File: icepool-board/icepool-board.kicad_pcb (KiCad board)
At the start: 4 copper layers, 90 x 40 mm, 103 parts, among them J2 PWR_IN, J3 I2C, J4 SWD, J5 8P8C_Shielded, J6 8P8C_Shielded, J7 USB_B_Micro, SW1 B3U-1000P, U1 LD1117S33CTR, U2 LD1117S12CTR, U3 ATSAMD21E, U4 ISL83488/ISL83490, U5 iCE40HX8K-BG121(121-Ball_caBG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, U6 iCE40HX8K-BG121(121-Ball_caBG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, X1 CB3LV-3I-16M0000, Y1 16MHz

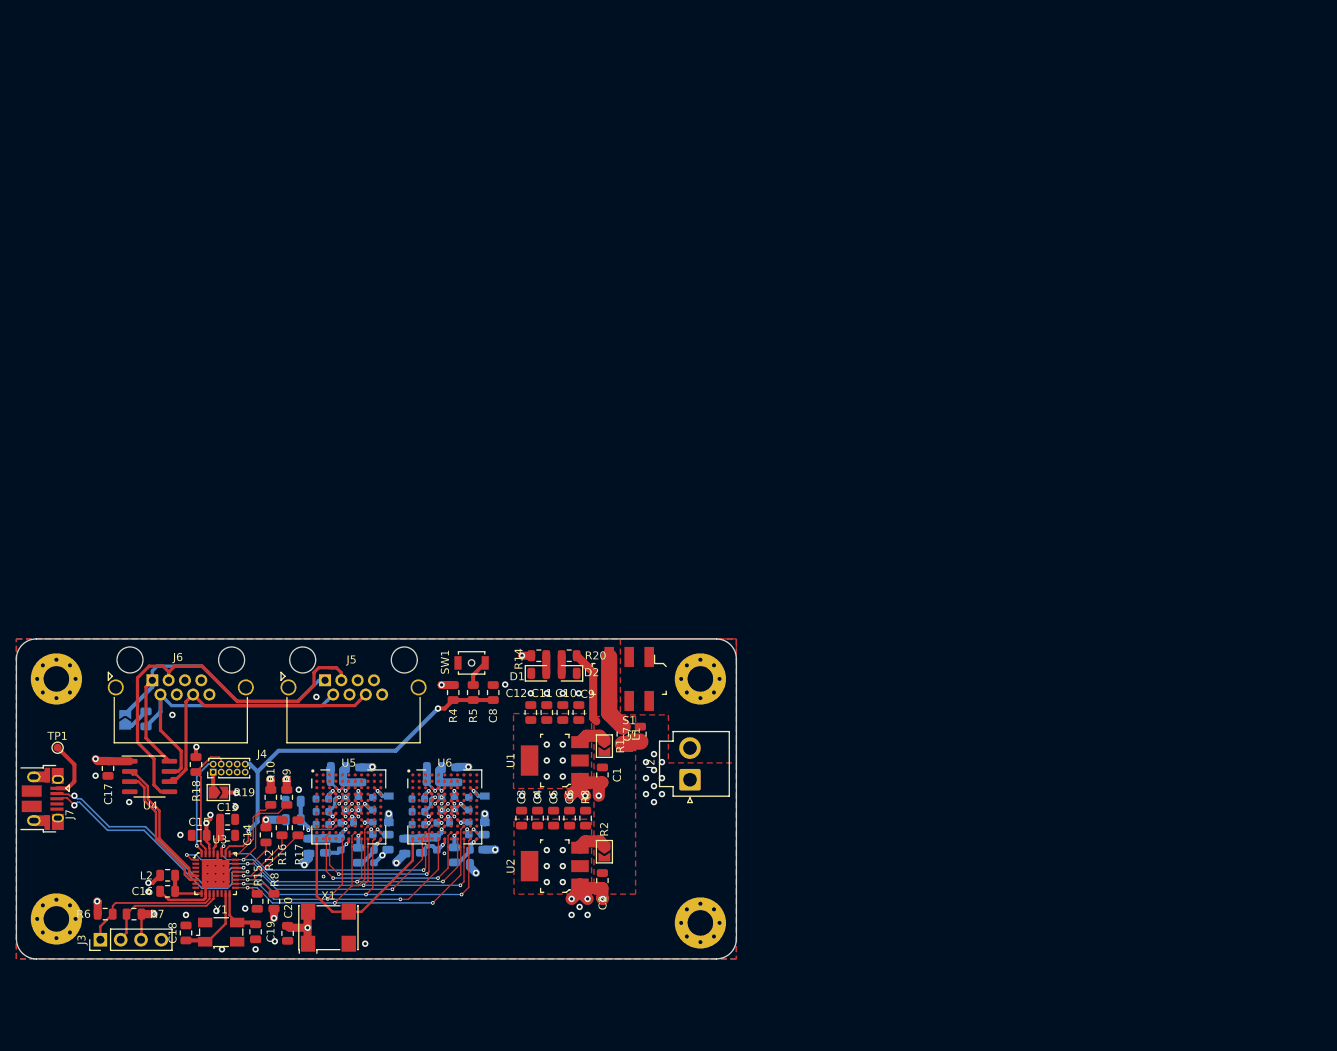
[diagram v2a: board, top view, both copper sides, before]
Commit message: Many updates, needs re-routing:
* Added two ICE40HX8K's.
* Changed ICE40 pinout to make routing more straightforward.
* Most inputs to ICE40 are now global fabric -- why not?
* Added CRESET_B to each FPGA, allowing for per-FPGA bitstreams.
* Replaced LDOs with beefier ones
* Added second +1.2V rail.
* Replaced many passives with 0402's.

Possible future changes:

* New CRESET_B use the remaining pins on SAMD21, may upgrade to 48pin.
* May add external flash or upgrade to SAMD51 for additional bitstream
storage.
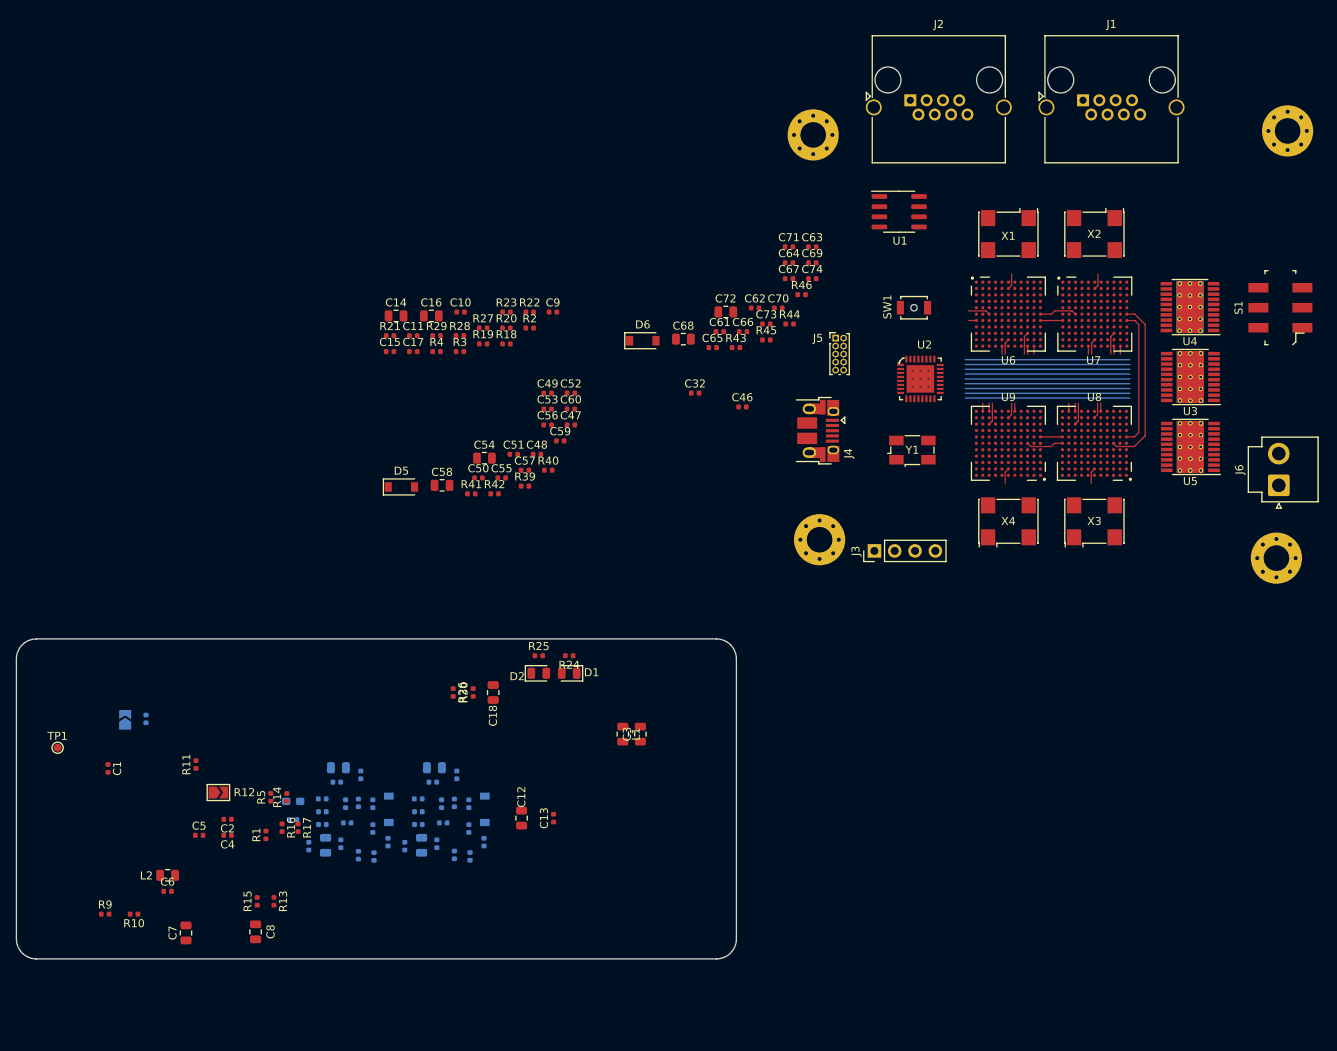
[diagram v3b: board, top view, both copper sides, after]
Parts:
- removed the C1 at (103.2, 97.0)
- removed the C12 at (94.3, 89.2)
- removed the C2 at (103.2, 110.2)
- removed the C29 at (71.2, 100.6)
- removed the C4 at (95.2, 102.4)
- removed the C6 at (99.2, 102.4)
- removed the J4 at (54.6, 96.7)
- removed the J6 at (47.0, 85.2)
- removed the R1 at (103.5, 93.4)
- removed the U1 at (97.3, 95.2)
- added C14: 10uF, Capacitor_SMD:C_0805_2012Metric, F.Cu at (77.5, 39.6)
- added C15: 0.1uF, Capacitor_SMD:C_0402_1005Metric, F.Cu at (76.7, 44.1)
- added C16: 10uF, Capacitor_SMD:C_0805_2012Metric, F.Cu at (81.9, 39.6)
- added C17: 0.1uF, Capacitor_SMD:C_0402_1005Metric, F.Cu at (79.6, 44.1)
- added C32: 0.01u, Capacitor_SMD:C_0402_1005Metric, F.Cu at (114.8, 49.3)
- added C46: 0.01u, Capacitor_SMD:C_0402_1005Metric, F.Cu at (120.8, 51.0)
- added C47: 0.1uF, Capacitor_SMD:C_0402_1005Metric, F.Cu at (99.3, 53.3)
- added C48: 0.1uF, Capacitor_SMD:C_0402_1005Metric, F.Cu at (95.1, 56.9)
- added C49: 0.1uF, Capacitor_SMD:C_0402_1005Metric, F.Cu at (96.4, 49.3)
- added C50: 0.1uF, Capacitor_SMD:C_0402_1005Metric, F.Cu at (87.8, 59.9)
- added C51: 0.1uF, Capacitor_SMD:C_0402_1005Metric, F.Cu at (92.2, 56.9)
- added C52: 0.1uF, Capacitor_SMD:C_0402_1005Metric, F.Cu at (99.3, 49.3)
- added C53: 0.1uF, Capacitor_SMD:C_0402_1005Metric, F.Cu at (96.4, 51.3)
- added C54: 10uF, Capacitor_SMD:C_0805_2012Metric, F.Cu at (88.5, 57.4)
- added C55: 0.1uF, Capacitor_SMD:C_0402_1005Metric, F.Cu at (90.7, 59.9)
- added C56: 0.1uF, Capacitor_SMD:C_0402_1005Metric, F.Cu at (96.4, 53.3)
- added C57: 0.1uF, Capacitor_SMD:C_0402_1005Metric, F.Cu at (93.6, 58.9)
- added C58: 10uF, Capacitor_SMD:C_0805_2012Metric, F.Cu at (83.2, 60.8)
- added C59: 0.1uF, Capacitor_SMD:C_0402_1005Metric, F.Cu at (98.0, 55.2)
- added C60: 0.01u, Capacitor_SMD:C_0402_1005Metric, F.Cu at (99.3, 51.3)
- added C61: 0.1uF, Capacitor_SMD:C_0402_1005Metric, F.Cu at (117.9, 41.6)
- added C62: 0.1uF, Capacitor_SMD:C_0402_1005Metric, F.Cu at (122.3, 38.6)
- added C63: 0.1uF, Capacitor_SMD:C_0402_1005Metric, F.Cu at (129.5, 31.0)
- added C64: 0.1uF, Capacitor_SMD:C_0402_1005Metric, F.Cu at (126.6, 33.0)
- added C65: 0.1uF, Capacitor_SMD:C_0402_1005Metric, F.Cu at (117.0, 43.6)
- added C66: 0.1uF, Capacitor_SMD:C_0402_1005Metric, F.Cu at (120.8, 41.6)
- added C67: 0.1uF, Capacitor_SMD:C_0402_1005Metric, F.Cu at (126.6, 35.0)
- added C68: 10uF, Capacitor_SMD:C_0805_2012Metric, F.Cu at (113.4, 42.5)
- added C69: 0.1uF, Capacitor_SMD:C_0402_1005Metric, F.Cu at (129.5, 33.0)
- added C70: 0.1uF, Capacitor_SMD:C_0402_1005Metric, F.Cu at (125.2, 38.6)
- added C71: 0.1uF, Capacitor_SMD:C_0402_1005Metric, F.Cu at (126.6, 31.0)
- added C72: 10uF, Capacitor_SMD:C_0805_2012Metric, F.Cu at (118.7, 39.1)
- added C73: 0.1uF, Capacitor_SMD:C_0402_1005Metric, F.Cu at (123.7, 40.6)
- added C74: 0.01u, Capacitor_SMD:C_0402_1005Metric, F.Cu at (129.5, 35.0)
- added D5: CDBU0520/MBR0520LT1G, Diode_SMD:D_SOD-123, F.Cu at (78.1, 61.0)
- added D6: CDBU0520/MBR0520LT1G, Diode_SMD:D_SOD-123, F.Cu at (108.3, 42.7)
- added J1: 8P8C_Shielded, Connector_RJ:RJ45_Amphenol_RJHSE5380, F.Cu at (163.3, 12.7)
- added J2: 8P8C_Shielded, Connector_RJ:RJ45_Amphenol_RJHSE5380, F.Cu at (141.7, 12.7)
- added R18: 196k, Resistor_SMD:R_0402_1005Metric, F.Cu at (91.3, 43.1)
- added R19: 8k, Resistor_SMD:R_0402_1005Metric, F.Cu at (88.3, 43.1)
- added R20: 8k, Resistor_SMD:R_0402_1005Metric, F.Cu at (91.3, 41.1)
- added R21: 110k, Resistor_SMD:R_0402_1005Metric, F.Cu at (76.7, 42.1)
- added R22: 110k, Resistor_SMD:R_0402_1005Metric, F.Cu at (94.2, 39.1)
- added R23: 110k, Resistor_SMD:R_0402_1005Metric, F.Cu at (91.3, 39.1)
- added R27: 250k, Resistor_SMD:R_0402_1005Metric, F.Cu at (88.3, 41.1)
- added R28: 250k, Resistor_SMD:R_0402_1005Metric, F.Cu at (85.4, 42.1)
- added R29: 250k, Resistor_SMD:R_0402_1005Metric, F.Cu at (82.5, 42.1)
- added R39: 100R, Resistor_SMD:R_0402_1005Metric, F.Cu at (93.6, 60.9)
- added R4: 4k7, Resistor_SMD:R_0402_1005Metric, F.Cu at (82.5, 44.1)
- added R40: 100R, Resistor_SMD:R_0402_1005Metric, F.Cu at (96.5, 58.9)
- added R41: 4k7, Resistor_SMD:R_0402_1005Metric, F.Cu at (86.9, 61.9)
- added R42: 4k7, Resistor_SMD:R_0402_1005Metric, F.Cu at (89.8, 61.9)
- added R43: 100R, Resistor_SMD:R_0402_1005Metric, F.Cu at (119.9, 43.6)
- added R44: 100R, Resistor_SMD:R_0402_1005Metric, F.Cu at (126.7, 40.6)
- added R45: 4k7, Resistor_SMD:R_0402_1005Metric, F.Cu at (123.7, 42.6)
- added R46: 4k7, Resistor_SMD:R_0402_1005Metric, F.Cu at (128.2, 37.0)
- added U4: TPS77801_HTSSOP20, Package_SO:HTSSOP-20-1EP_4.4x6.5mm_P0.65mm_EP3.4x6.5mm_ThermalVias, F.Cu at (176.7, 38.5)
- added U7: iCE40HX8K-BG121(121-Ball_caBGA), icepool-library:BGA-121_11x11_9.0x9.0mm, F.Cu at (164.8, 39.4)
- added U8: iCE40HX8K-BG121(121-Ball_caBGA), icepool-library:BGA-121_11x11_9.0x9.0mm, F.Cu at (164.8, 55.5)
- added U9: iCE40HX8K-BG121(121-Ball_caBGA), icepool-library:BGA-121_11x11_9.0x9.0mm, F.Cu at (154.0, 55.5)
- added X2: CB3LV-3I-16M0000, Oscillator:Oscillator_SMD_Abracon_ASV-4Pin_7.0x5.1mm, F.Cu at (164.8, 29.4)
- added X3: CB3LV-3I-16M0000, Oscillator:Oscillator_SMD_Abracon_ASV-4Pin_7.0x5.1mm, F.Cu at (164.8, 65.3)
- added X4: CB3LV-3I-16M0000, Oscillator:Oscillator_SMD_Abracon_ASV-4Pin_7.0x5.1mm, F.Cu at (154.0, 65.3)
- C1: renamed from C17; footprint Capacitor_SMD:C_0805_2012Metric -> Capacitor_SMD:C_0402_1005Metric
- C10: value 1uF -> 0.1uF; footprint Capacitor_SMD:C_0805_2012Metric -> Capacitor_SMD:C_0402_1005Metric
- C11: footprint Capacitor_SMD:C_0805_2012Metric -> Capacitor_SMD:C_0402_1005Metric
- C13: renamed from C5; footprint Capacitor_SMD:C_0805_2012Metric -> Capacitor_SMD:C_0402_1005Metric
- C19: renamed from C21; footprint Capacitor_SMD:C_0603_1608Metric -> Capacitor_SMD:C_0402_1005Metric
- C2: renamed from C13; footprint Capacitor_SMD:C_0805_2012Metric -> Capacitor_SMD:C_0402_1005Metric
- C20: value 0.01u -> 0.1uF; footprint Capacitor_SMD:C_0805_2012Metric -> Capacitor_SMD:C_0402_1005Metric; moved to B.Cu
- C21: renamed from C33; footprint Capacitor_SMD:C_0603_1608Metric -> Capacitor_SMD:C_0402_1005Metric
- C22: renamed from C24; footprint Capacitor_SMD:C_0603_1608Metric -> Capacitor_SMD:C_0402_1005Metric
- C23: renamed from C30; footprint Capacitor_SMD:C_0603_1608Metric -> Capacitor_SMD:C_0402_1005Metric
- C24: renamed from C27; footprint Capacitor_SMD:C_0603_1608Metric -> Capacitor_SMD:C_0402_1005Metric
- C25: renamed from C31; footprint Capacitor_SMD:C_0603_1608Metric -> Capacitor_SMD:C_0402_1005Metric
- C27: renamed from C23; footprint Capacitor_SMD:C_0603_1608Metric -> Capacitor_SMD:C_0402_1005Metric
- C28: footprint Capacitor_SMD:C_0603_1608Metric -> Capacitor_SMD:C_0402_1005Metric
- C29: renamed from C32; footprint Capacitor_SMD:C_0603_1608Metric -> Capacitor_SMD:C_0402_1005Metric
- C31: renamed from C26; footprint Capacitor_SMD:C_0603_1608Metric -> Capacitor_SMD:C_0402_1005Metric
- C33: renamed from C34; footprint Capacitor_SMD:C_0603_1608Metric -> Capacitor_SMD:C_0402_1005Metric
- C34: renamed from C42; footprint Capacitor_SMD:C_0603_1608Metric -> Capacitor_SMD:C_0402_1005Metric
- C35: renamed from C46; footprint Capacitor_SMD:C_0603_1608Metric -> Capacitor_SMD:C_0402_1005Metric
- C36: renamed from C37; footprint Capacitor_SMD:C_0603_1608Metric -> Capacitor_SMD:C_0402_1005Metric
- C37: renamed from C43; footprint Capacitor_SMD:C_0603_1608Metric -> Capacitor_SMD:C_0402_1005Metric
- C38: renamed from C40; footprint Capacitor_SMD:C_0603_1608Metric -> Capacitor_SMD:C_0402_1005Metric
- C39: renamed from C44; footprint Capacitor_SMD:C_0603_1608Metric -> Capacitor_SMD:C_0402_1005Metric
- C4: renamed from C14; footprint Capacitor_SMD:C_0805_2012Metric -> Capacitor_SMD:C_0402_1005Metric
- C41: renamed from C36; footprint Capacitor_SMD:C_0603_1608Metric -> Capacitor_SMD:C_0402_1005Metric
- C42: renamed from C41; footprint Capacitor_SMD:C_0603_1608Metric -> Capacitor_SMD:C_0402_1005Metric
- C43: renamed from C45; footprint Capacitor_SMD:C_0603_1608Metric -> Capacitor_SMD:C_0402_1005Metric
- C45: renamed from C39; footprint Capacitor_SMD:C_0603_1608Metric -> Capacitor_SMD:C_0402_1005Metric
- C5: renamed from C15; footprint Capacitor_SMD:C_0805_2012Metric -> Capacitor_SMD:C_0402_1005Metric
- C6: renamed from C16; footprint Capacitor_SMD:C_0805_2012Metric -> Capacitor_SMD:C_0402_1005Metric
- C9: value 10uF -> 0.1uF; footprint Capacitor_SMD:C_0805_2012Metric -> Capacitor_SMD:C_0402_1005Metric
- J5: value 8P8C_Shielded -> SWD; footprint icepool-library:RJ45_Amphenol_RJHSE5380 -> Connector_PinHeader_1.00mm:PinHeader_2x05_P1.00mm_Vertical
- R1: renamed from R12; footprint Resistor_SMD:R_0805_2012Metric -> Resistor_SMD:R_0402_1005Metric
- R10: renamed from R7; footprint Resistor_SMD:R_0805_2012Metric -> Resistor_SMD:R_0402_1005Metric
- R11: renamed from R18; footprint Resistor_SMD:R_0805_2012Metric -> Resistor_SMD:R_0402_1005Metric
- R13: renamed from R8; footprint Resistor_SMD:R_0805_2012Metric -> Resistor_SMD:R_0402_1005Metric
- R14: renamed from R9; footprint Resistor_SMD:R_0805_2012Metric -> Resistor_SMD:R_0402_1005Metric
- R15, R16, R17: footprint Resistor_SMD:R_0805_2012Metric -> Resistor_SMD:R_0402_1005Metric
- R2: value 0R -> 4k7; footprint Jumper:SolderJumper-2_P1.3mm_Open_TrianglePad1.0x1.5mm -> Resistor_SMD:R_0402_1005Metric
- R24: renamed from R20; footprint Resistor_SMD:R_0805_2012Metric -> Resistor_SMD:R_0402_1005Metric
- R25: renamed from R14; footprint Resistor_SMD:R_0805_2012Metric -> Resistor_SMD:R_0402_1005Metric
- R26: renamed from R4; footprint Resistor_SMD:R_0805_2012Metric -> Resistor_SMD:R_0402_1005Metric
- R3: value 120R -> 4k7; footprint Resistor_SMD:R_0805_2012Metric -> Resistor_SMD:R_0402_1005Metric
- R30: renamed from R5; footprint Resistor_SMD:R_0805_2012Metric -> Resistor_SMD:R_0402_1005Metric
- R31: renamed from R23; value 120R -> 100R; footprint Resistor_SMD:R_0805_2012Metric -> Resistor_SMD:R_0402_1005Metric
- R32: renamed from R24; value 120R -> 100R; footprint Resistor_SMD:R_0805_2012Metric -> Resistor_SMD:R_0402_1005Metric
- R33: renamed from R25; footprint Resistor_SMD:R_0805_2012Metric -> Resistor_SMD:R_0402_1005Metric
- R34: renamed from R26; footprint Resistor_SMD:R_0805_2012Metric -> Resistor_SMD:R_0402_1005Metric
- R35: renamed from R27; value 120R -> 100R; footprint Resistor_SMD:R_0805_2012Metric -> Resistor_SMD:R_0402_1005Metric
- R36: renamed from R28; value 120R -> 100R; footprint Resistor_SMD:R_0805_2012Metric -> Resistor_SMD:R_0402_1005Metric
- R37: renamed from R29; footprint Resistor_SMD:R_0805_2012Metric -> Resistor_SMD:R_0402_1005Metric
- R38: renamed from R30; footprint Resistor_SMD:R_0805_2012Metric -> Resistor_SMD:R_0402_1005Metric
- R5: renamed from R10; footprint Resistor_SMD:R_0805_2012Metric -> Resistor_SMD:R_0402_1005Metric
- R6: renamed from R11; footprint Resistor_SMD:R_0805_2012Metric -> Resistor_SMD:R_0402_1005Metric
- R7: renamed from R21; footprint Resistor_SMD:R_0805_2012Metric -> Resistor_SMD:R_0402_1005Metric
- R8: renamed from R13; footprint Resistor_SMD:R_0805_2012Metric -> Resistor_SMD:R_0603_1608Metric_Pad1.05x0.95mm_HandSolder
- R9: renamed from R6; footprint Resistor_SMD:R_0805_2012Metric -> Resistor_SMD:R_0402_1005Metric
- U2: value LD1117S12CTR -> ATSAMD21E; footprint digikey-footprints:SOT-223 -> digikey-footprints:QFN-32-1EP_5x5mm
- U3: value ATSAMD21E -> TPS77801_HTSSOP20; footprint digikey-footprints:QFN-32-1EP_5x5mm -> Package_SO:HTSSOP-20-1EP_4.4x6.5mm_P0.65mm_EP3.4x6.5mm_ThermalVias
- U5: value iCE40HX8K-BG121(121-Ball_caBGA) -> TPS77801_HTSSOP20; footprint icepool-library:BGA-121_11x11_9.0x9.0mm -> Package_SO:HTSSOP-20-1EP_4.4x6.5mm_P0.65mm_EP3.4x6.5mm_ThermalVias
- moved U3 136.5 mm to (176.8, 47.3), turned to 180 degrees
- moved X1 121.4 mm to (154.0, 29.4), turned to 180 degrees
- moved U1 117.3 mm to (140.3, 26.6)
- moved H2 116.5 mm to (129.6, 17.0)
- moved U5 114.4 mm to (176.8, 56.0), turned to 180 degrees
- moved J3 108.3 mm to (137.2, 69.0)
- moved J4 107.3 mm to (130.2, 54.0)
- moved H1 106.5 mm to (130.4, 67.6)
- moved Y1 105.3 mm to (142.0, 56.4)
- moved H4 100.4 mm to (188.9, 16.5)
- moved S1 93.7 mm to (188.0, 38.6), turned to 90 degrees
- moved U6 93.6 mm to (154.0, 39.4)
- moved H3 85.2 mm to (187.5, 69.9)
- moved J6 82.3 mm to (187.8, 60.8)
- moved J5 76.8 mm to (132.4, 42.4)
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- renumbered C3 to C12, C8 to C18, C22 to C26, C7 to C3, C25 to C30, C35 to C40, C38 to C44, C18 to C7, C19 to C8, D2 to D1, D1 to D2, J7 to J4, J2 to J6, R19 to R12, U4 to U1
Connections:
- C10 pad 1: +3V3 -> VCC
- C11 pad 1: +3V3 -> VCC
- C12 pad 1: +1V2 -> +3V3
- C13 pad 1: +1V2 -> +3V3
- C19 pad 2: +1V2 -> +1V2_0
- C22 pad 2: +1V2 -> +1V2_0
- C24 pad 2: +1V2 -> +1V2_0
- C28 pad 2: +1V2 -> +1V2_0
- C33 pad 2: +1V2 -> +1V2_0
- C36 pad 2: +1V2 -> +1V2_0
- C38 pad 2: +1V2 -> +1V2_0
- C42 pad 2: +1V2 -> +1V2_0
- C9 pad 1: +3V3 -> VCC
- J3 pad 1: /SDA -> /I2C_SDA
- J3 pad 2: /SCL -> /I2C_SCL
- J4 pad 4: Net-(J7-Pad4) -> (no net)
- J4 pad 6: GND -> Net-(J4-Pad6)
- J5 pad 1: /RX+ -> Net-(J5-Pad1)
- J5 pad 2: /RX- -> /SWD_IO
- J5 pad 3: /TX+ -> GND
- J5 pad 4: Net-(J5-Pad4) -> /SWD_CLK
- J5 pad 5: Net-(J5-Pad5) -> GND
- J5 pad 6: /TX- -> (no net)
- J5 pad 7: Net-(J5-Pad7) -> GND
- J5 pad 8: Net-(J5-Pad8) -> (no net)
- R1 pad 1: /CRESET_B -> /CRESET_B_0
- R10 pad 2: /SCL -> /I2C_SCL
- R12 pad 1: Net-(J4-Pad1) (its old number) -> Net-(J5-Pad1)
- R2 pad 1: Net-(R2-Pad1) -> /CRESET_B_1
- R2 pad 2: VCC -> +3V3
- R3 pad 1: +1V2 -> /CRESET_B_2
- R3 pad 2: GND -> +3V3
- R33 pad 2: /ICE40HX8K-BG121_0/CDONE -> Net-(R33-Pad2)
- R37 pad 2: /ICE40HX8K-BG121_1/CDONE -> Net-(R37-Pad2)
- R5 pad 1: /READY -> GND
- R5 pad 2: +3V3 -> /READY
- R9 pad 2: /SDA -> /I2C_SDA
- S1 pad 1: Net-(S1-Pad1) -> (no net)
- S1 pad 4: Net-(S1-Pad4) -> (no net)
- U2 pad 1: GND -> /CRESET_B_0
- U2 pad 2: +1V2 -> /CRESET_B_1
- U2 pad 3: Net-(R2-Pad1) -> /CRESET_B_2
- U2 pad 4: +1V2 -> /CRESET_B_3
- U3 pad 1: /CRESET_B -> GND
- U3 pad 11: /SDA -> GND
- U3 pad 12: /SCL -> GND
- U3 pad 13: Net-(U3-Pad13) -> +3V3
- U3 pad 14: Net-(U3-Pad14) -> +3V3
- U3 pad 15: /XIN -> Net-(R18-Pad2)
- U3 pad 16: /XOUT -> PG_0
- U3 pad 17: /MOSI -> (no net)
- U3 pad 18: /~WE -> (no net)
- U3 pad 19: /SCK -> GND
- U3 pad 2: Net-(U3-Pad2) -> GND
- U3 pad 20: /MISO -> GND
- U3 pad 21: /USB_D+ -> GND
- U3 pad 3: Net-(U3-Pad3) -> GND
- U3 pad 4: Net-(U3-Pad4) -> (no net)
- U3 pad 5: /RX -> GND
- U3 pad 6: /TX -> VCC
- U3 pad 7: Net-(U3-Pad7) -> VCC
- U3 pad 8: Net-(U3-Pad8) -> (no net)
- U3 pad 9: /VDDANA -> GND
- U6 pad A1: Net-(U6-PadA1) -> (no net)
- U6 pad A10: Net-(U6-PadA10) -> (no net)
- U6 pad A11: Net-(U6-PadA11) -> (no net)
- U6 pad A2: Net-(U6-PadA2) -> (no net)
- U6 pad A3: Net-(U6-PadA3) -> (no net)
- U6 pad A4: Net-(U6-PadA4) -> (no net)
- U6 pad A5: Net-(U6-PadA5) -> (no net)
- U6 pad A6: Net-(U6-PadA6) -> (no net)
- U6 pad A7: Net-(U6-PadA7) -> (no net)
- U6 pad A8: Net-(U6-PadA8) -> (no net)
- U6 pad A9: Net-(U6-PadA9) -> (no net)
- U6 pad B1: Net-(U6-PadB1) -> (no net)
- U6 pad B10: Net-(U6-PadB10) -> (no net)
- U6 pad B11: Net-(U6-PadB11) -> (no net)
- U6 pad B2: Net-(U6-PadB2) -> (no net)
- U6 pad B3: Net-(U6-PadB3) -> (no net)
- U6 pad B4: Net-(U6-PadB4) -> (no net)
- U6 pad B5: Net-(U6-PadB5) -> (no net)
- U6 pad B6: Net-(U6-PadB6) -> /ICE40HX8K-BG121_0/CLK
- U6 pad B7: Net-(U6-PadB7) -> (no net)
- U6 pad B8: Net-(U6-PadB8) -> (no net)
- U6 pad B9: Net-(U6-PadB9) -> (no net)
- U6 pad C1: Net-(U6-PadC1) -> (no net)
- U6 pad C10: /ICE40HX8K-BG121_1/VPP_2V5 -> /ICE40HX8K-BG121_0/VPP_2V5
- U6 pad C11: Net-(U6-PadC11) -> (no net)
- U6 pad C2: Net-(U6-PadC2) -> (no net)
- U6 pad C3: Net-(U6-PadC3) -> (no net)
- U6 pad C4: Net-(U6-PadC4) -> (no net)
- U6 pad C5: /ICE40HX8K-BG121_1/GNDPLL1 -> /ICE40HX8K-BG121_0/GNDPLL1
- U6 pad C6: /ICE40HX8K-BG121_1/VCCPLL1 -> /ICE40HX8K-BG121_0/VCCPLL1
- U6 pad C7: Net-(U6-PadC7) -> (no net)
- U6 pad C8: Net-(U6-PadC8) -> (no net)
- U6 pad C9: Net-(U6-PadC9) -> (no net)
- U6 pad D1: Net-(U6-PadD1) -> (no net)
- U6 pad D10: Net-(U6-PadD10) -> (no net)
- U6 pad D11: Net-(U6-PadD11) -> (no net)
- U6 pad D2: Net-(U6-PadD2) -> (no net)
- U6 pad D3: Net-(U6-PadD3) -> (no net)
- U6 pad D4: +1V2 -> +1V2_0
- U6 pad D5: Net-(U6-PadD5) -> (no net)
- U6 pad D7: Net-(U6-PadD7) -> (no net)
- U6 pad D8: +1V2 -> +1V2_0
- U6 pad D9: Net-(U6-PadD9) -> (no net)
- U6 pad E1: Net-(U6-PadE1) -> (no net)
- U6 pad E10: Net-(U6-PadE10) -> (no net)
- U6 pad E11: Net-(U6-PadE11) -> (no net)
- U6 pad E2: Net-(U6-PadE2) -> (no net)
- U6 pad E3: Net-(U6-PadE3) -> (no net)
- U6 pad E8: Net-(U6-PadE8) -> (no net)
- U6 pad E9: Net-(U6-PadE9) -> (no net)
- U6 pad F1: Net-(U6-PadF1) -> (no net)
- U6 pad F10: Net-(U6-PadF10) -> (no net)
- U6 pad F11: Net-(U6-PadF11) -> /READY_0_1
- U6 pad F2: Net-(U6-PadF2) -> (no net)
- U6 pad F3: Net-(U6-PadF3) -> /READY_0
- U6 pad F4: Net-(U6-PadF4) -> (no net)
- U6 pad F9: Net-(U6-PadF9) -> (no net)
- U6 pad G1: Net-(U6-PadG1) -> /MOSI
- U6 pad G10: Net-(U6-PadG10) -> (no net)
- U6 pad G11: Net-(U6-PadG11) -> /FIFO_0_1
- U6 pad G2: Net-(U6-PadG2) -> (no net)
- U6 pad G3: Net-(U6-PadG3) -> (no net)
- U6 pad G8: Net-(U6-PadG8) -> (no net)
- U6 pad G9: Net-(U6-PadG9) -> (no net)
- U6 pad H1: Net-(U6-PadH1) -> (no net)
- U6 pad H10: Net-(U6-PadH10) -> (no net)
- U6 pad H11: Net-(U6-PadH11) -> (no net)
- U6 pad H2: Net-(U6-PadH2) -> (no net)
- U6 pad H3: Net-(U6-PadH3) -> (no net)
- U6 pad H4: +1V2 -> +1V2_0
- U6 pad H7: Net-(U6-PadH7) -> (no net)
- U6 pad H8: +1V2 -> +1V2_0
- U6 pad H9: Net-(U6-PadH9) -> (no net)
- U6 pad J1: Net-(U6-PadJ1) -> (no net)
- U6 pad J10: Net-(U6-PadJ10) -> (no net)
- U6 pad J11: Net-(U6-PadJ11) -> (no net)
- U6 pad J2: Net-(U6-PadJ2) -> (no net)
- U6 pad J3: Net-(U6-PadJ3) -> (no net)
- U6 pad J4: /READY_0_1 -> (no net)
- U6 pad J5: Net-(U6-PadJ5) -> (no net)
- U6 pad J6: /ICE40HX8K-BG121_1/VCCPLL0 -> /ICE40HX8K-BG121_0/VCCPLL0
- U6 pad J7: Net-(U6-PadJ7) -> (no net)
- U6 pad J8: Net-(U6-PadJ8) -> (no net)
- U6 pad K1: Net-(U6-PadK1) -> (no net)
- U6 pad K10: /ICE40HX8K-BG121_1/SPI_SS_B -> /ICE40HX8K-BG121_0/SPI_SS_B
- U6 pad K11: Net-(U6-PadK11) -> (no net)
- U6 pad K2: Net-(U6-PadK2) -> (no net)
- U6 pad K3: /MISO -> (no net)
- U6 pad K4: Net-(U6-PadK4) -> (no net)
- U6 pad K5: Net-(U6-PadK5) -> (no net)
- U6 pad K6: Net-(U6-PadK6) -> /~GS
- U6 pad K7: /FIFO_0_1 -> (no net)
- U6 pad K8: /ICE40HX8K-BG121_1/CDONE -> Net-(R33-Pad2)
- U6 pad K9: /ICE40HX8K-BG121_1/GMISO -> (no net)
- U6 pad L1: /OSC -> (no net)
- U6 pad L2: Net-(U6-PadL2) -> (no net)
- U6 pad L3: /READY -> (no net)
- U6 pad L4: Net-(U6-PadL4) -> (no net)
- U6 pad L6: /ICE40HX8K-BG121_1/GNDPLL0 -> /ICE40HX8K-BG121_0/GNDPLL0
- U6 pad L7: Net-(U6-PadL7) -> (no net)
- U6 pad L8: /~GS -> (no net)
- U6 pad L9: /CRESET_B -> /CRESET_B_0
- X1 pad 3: /OSC -> /ICE40HX8K-BG121_0/CLK
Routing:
- net +1V2: track 95.2 -> 0.00 mm, vias 18 -> 0
- net +3V3: track 64.8 -> 0.00 mm, vias 35 -> 0
- net /CRESET_B: track 53.1 -> 0.00 mm, vias 4 -> 0
- net GND: track 52.1 -> 0.00 mm, vias 69 -> 0
- net /TX+: track 50.4 -> 0.00 mm
- net /~RESET: track 47.9 -> 0.00 mm, vias 2 -> 0
- net /RX+: track 43.2 -> 0.00 mm
- net /RX-: track 39.4 -> 0.00 mm
- net /READY: track 37.7 -> 0.00 mm, vias 2 -> 0
- net /TX-: track 35.2 -> 0.00 mm
- net /USB_D+: track 32.1 -> 0.00 mm, vias 2 -> 0
- net /USB_D-: track 30.8 -> 0.00 mm, vias 2 -> 0
- net /SCK: track 52.4 -> 24.6 mm, vias 3 -> 0
- net /OSC: track 25.3 -> 0.00 mm
- net /~GS: track 53.4 -> 28.5 mm, vias 4 -> 0
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- removed copper zone on F.Cu, net +1V2
- removed copper zone on In1.Cu, net +1V2
- removed copper zone on F.Cu, net +3V3
- removed copper zone on In1.Cu, net +3V3
- removed copper zone on F.Cu, net /VPWR
- removed copper zone on B.Cu, net GND
- removed copper zone on F.Cu, net GND
- removed copper zone on In2.Cu, net GND
- removed copper zone on F.Cu, net VCC

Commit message: More work on layout. LDO may not cut it.
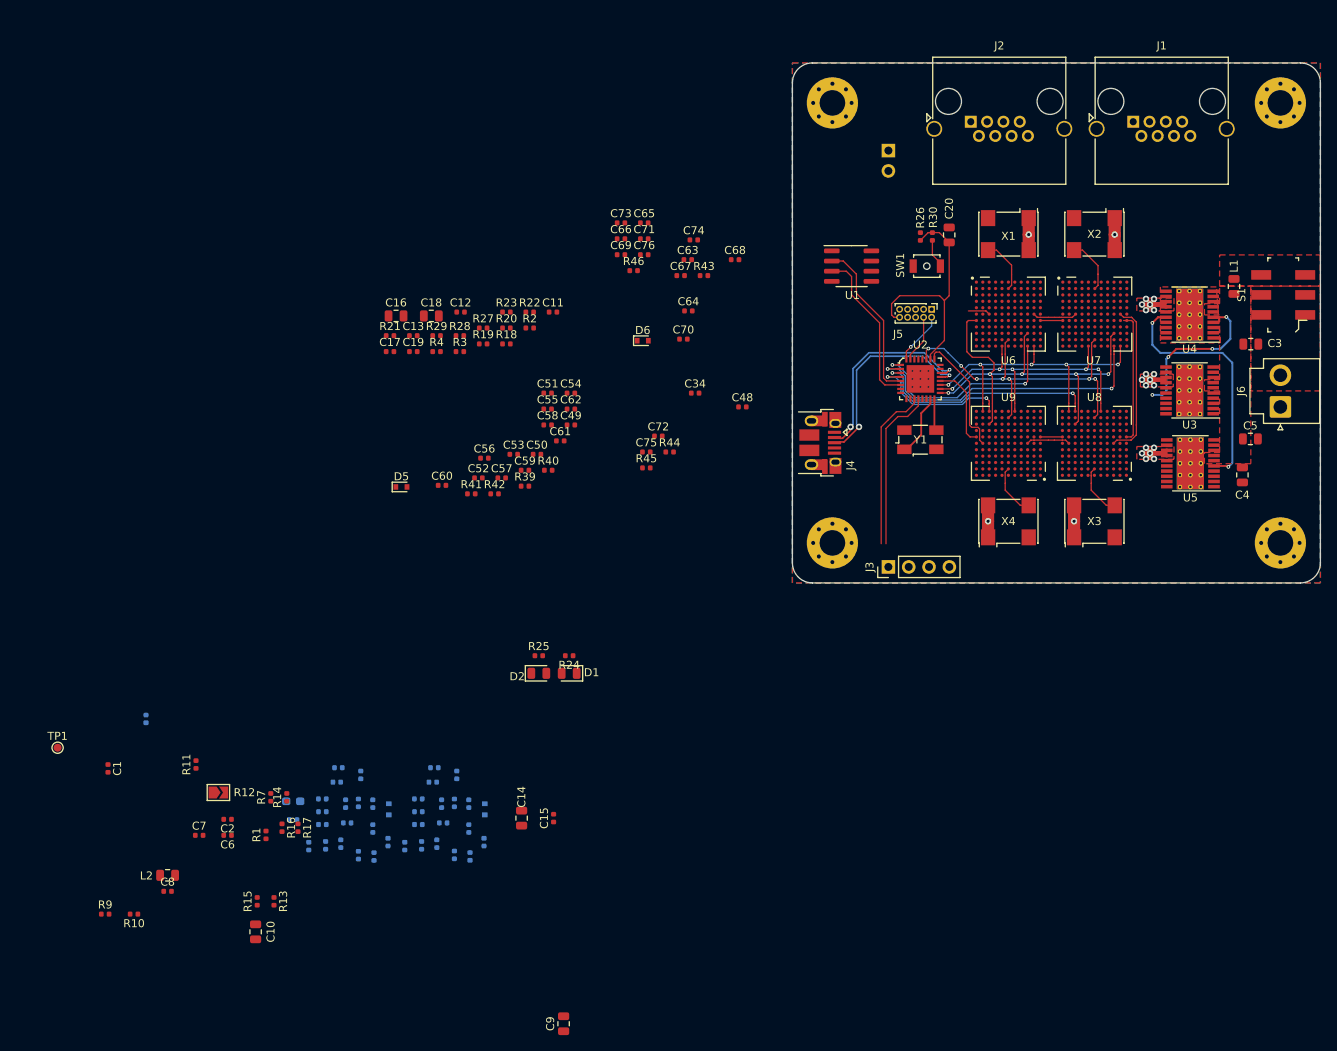
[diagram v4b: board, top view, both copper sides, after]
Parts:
- removed the C7 at (51.2, 116.8)
- added C4: 10uF, Capacitor_SMD:C_0805_2012Metric, F.Cu at (183.2, 59.5)
- added C5: 10uF, Capacitor_SMD:C_0805_2012Metric, F.Cu at (184.2, 55.0)
- added C9: 10pF, Capacitor_SMD:C_0805_2012Metric, F.Cu at (98.4, 128.1)
- C28: renamed from C26; footprint Capacitor_SMD:C_0805_2012Metric -> Capacitor_SMD:C_0402_1005Metric
- C32: renamed from C30; footprint Capacitor_SMD:C_0805_2012Metric -> Capacitor_SMD:C_0402_1005Metric
- C42: renamed from C40; footprint Capacitor_SMD:C_0805_2012Metric -> Capacitor_SMD:C_0402_1005Metric
- C46: renamed from C44; footprint Capacitor_SMD:C_0805_2012Metric -> Capacitor_SMD:C_0402_1005Metric
- C56: renamed from C54; footprint Capacitor_SMD:C_0805_2012Metric -> Capacitor_SMD:C_0402_1005Metric
- C60: renamed from C58; footprint Capacitor_SMD:C_0805_2012Metric -> Capacitor_SMD:C_0402_1005Metric
- C70: renamed from C68; footprint Capacitor_SMD:C_0805_2012Metric -> Capacitor_SMD:C_0402_1005Metric
- C74: renamed from C72; footprint Capacitor_SMD:C_0805_2012Metric -> Capacitor_SMD:C_0402_1005Metric
- D3, D4, D5, D6: footprint Diode_SMD:D_SOD-123 -> Diode_SMD:D_SOD-523
- JP1: footprint Jumper:SolderJumper-2_P1.3mm_Open_TrianglePad1.0x1.5mm -> Connector_PinHeader_2.54mm:PinHeader_1x02_P2.54mm_Vertical
- moved JP1 119.0 mm to (139.0, 19.0), turned to 180 degrees
- moved L1 94.7 mm to (182.2, 35.9)
- moved C3 90.5 mm to (184.3, 43.1), turned to 0 degrees
- moved R26 81.6 mm to (143.0, 29.7)
- moved R30 80.9 mm to (144.5, 29.7), turned to 270 degrees
- moved C20 80.8 mm to (146.6, 29.5)
- moved H1 54.6 mm to (132.0, 13.0)
- moved H2 51.1 mm to (132.0, 68.0)
- moved C72 21.9 mm to (110.2, 54.6)
- moved C75 21.9 mm to (108.7, 56.6)
- moved R44 21.9 mm to (111.7, 56.6)
- moved R45 21.9 mm to (108.7, 58.6)
- moved C65 21.2 mm to (108.5, 28.0)
- moved C71 21.2 mm to (108.5, 30.0)
- moved C76 21.2 mm to (108.5, 32.0)
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- renumbered C8 to C10, C9 to C11, C10 to C12, C11 to C13, C12 to C14, C13 to C15, C14 to C16, C15 to C17, C16 to C18, C17 to C19, C18 to C20, C19 to C21, C20 to C22, C21 to C23, C22 to C24, C23 to C25, C24 to C26, C25 to C27, C27 to C29, C28 to C30, C29 to C31, C31 to C33, C32 to C34, C33 to C35, C34 to C36, C35 to C37, C36 to C38, C37 to C39, C38 to C40, C39 to C41, C41 to C43, C42 to C44, C43 to C45, C45 to C47, C46 to C48, C47 to C49, C48 to C50, C49 to C51, C50 to C52, C51 to C53, C52 to C54, C53 to C55, C55 to C57, C56 to C58, C57 to C59, C4 to C6, C59 to C61, C60 to C62, C61 to C63, C62 to C64, C63 to C65, C64 to C66, C65 to C67, C66 to C68, C67 to C69, C5 to C7, C69 to C71, C70 to C72, C71 to C73, C73 to C75, C74 to C76, C6 to C8, R6 to R5, R7 to R6, R5 to R7
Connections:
- U2 pad 12: (no net) -> /I2C_SCL
- U6 pad F10: (no net) -> /READY_0_1
- U6 pad F11: /READY_0_1 -> (no net)
- U7 pad F10: (no net) -> /READY_1_2
- U7 pad F11: /READY_1_2 -> (no net)
- U8 pad F10: (no net) -> /READY_2_3
- U8 pad F11: /READY_2_3 -> (no net)
- U9 pad F10: (no net) -> /READY
- U9 pad F11: /READY -> (no net)
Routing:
- net PG_1: track 0.00 -> 30.7 mm, vias 0 -> 2
- net /~RESET: track 0.00 -> 29.9 mm
- net /USB_D+: track 0.00 -> 25.7 mm, vias 0 -> 2
- net /USB_D-: track 0.00 -> 25.6 mm, vias 0 -> 2
- net +3V3: track 0.00 -> 24.7 mm, vias 0 -> 10
- net /MOSI: track 32.7 -> 56.4 mm, vias 0 -> 5
- net /I2C_SDA: track 0.00 -> 20.5 mm
- net /I2C_SCL: track 0.00 -> 20.5 mm
- net /RX: track 0.00 -> 20.4 mm
- net /TX: track 0.00 -> 20.0 mm
- net PG_0: track 0.00 -> 19.6 mm, vias 0 -> 4
- net /CRESET_B_1: track 21.6 -> 38.3 mm, vias 0 -> 2
- net /~GS: track 28.5 -> 44.6 mm, vias 0 -> 7
- net /SCK: track 24.6 -> 40.3 mm, vias 0 -> 5
- net /READY: track 0.00 -> 15.5 mm
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- added copper zone on F.Cu, net (none)
- added copper zone on F.Cu, net +1V2_0
- added copper zone on In2.Cu, net +1V2_0
- added copper zone on F.Cu, net +1V2_1
- added copper zone on In2.Cu, net +1V2_1
- added copper zone on F.Cu, net +3V3
- added copper zone on In2.Cu, net +3V3
- added copper zone on F.Cu, net /VPWR
- added copper zone on B.Cu, net GND
- added copper zone on F.Cu, net GND
- added copper zone on In1.Cu, net GND
- added copper zone on F.Cu, net Net-(L1-Pad1)
- added copper zone on F.Cu, net VCC
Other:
- board size 90 x 40 mm -> 66 x 65 mm
